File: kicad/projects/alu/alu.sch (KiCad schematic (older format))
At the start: 46 parts, among them J1 Conn_01x16_Female, J2 Conn_01x18_Female, J3 Control_signal_backplane, J4 Bus_connection, J5 Aux_connection, U1 74HCT04, U10 74HCT157, U11 74HCT157, U2 74LS181, U3 74LS181, U4 74HCT245, U5 74LS181, U6 74HCT245, U7 74LS181, U8 74HCT157, U9 74HCT157

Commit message: Add updated 74LS181 to eight bit symbol lib with open collector output. Mostly finish schematic. Little bit of PBC layout work.
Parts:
- removed U2, U3, U5, U7: 74LS181, Package_DIP:DIP-24_W15.24mm_Socket, symbol 74xx:74LS181
- added U2, U3, U5, U7: 74LS181, Package_DIP:DIP-24_W15.24mm_Socket, symbol eight-bit-computer:74LS181
- C1, C10, C11, C2, C3, C4, C5, C6, C7, C8, C9: footprint (none) -> Capacitor_THT:C_Disc_D4.7mm_W2.5mm_P5.00mm
- J1: value Conn_01x16_Female -> ACC_CONTENTS
- J2: value Conn_01x18_Female -> RES_AEQB_CRYBRW_OUT; footprint (none) -> Connector_PinSocket_2.54mm:PinSocket_1x18_P2.54mm_Horizontal
- R1: value R_US -> 1K; footprint (none) -> Resistor_THT:R_Axial_DIN0207_L6.3mm_D2.5mm_P10.16mm_Horizontal
- U10, U11, U8, U9: footprint Package_DIP:DIP-16_W7.62mm -> Package_DIP:DIP-16_W7.62mm_Socket
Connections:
- net labels added: ACC_00, ACC_01, ACC_02, ACC_03, ACC_04, ACC_05, ACC_06, ACC_07, ACC_08, ACC_09, ACC_10, ACC_11, ACC_12, ACC_13, ACC_14, ACC_15, A_EQ_B, A_IS_BUS, BUS_00, BUS_01, BUS_02, BUS_03, BUS_04, BUS_05, BUS_06, BUS_07, BUS_08, BUS_09, BUS_10, BUS_11, BUS_12, BUS_13, BUS_14, BUS_15, CARRY_BORROW_OUT, CARRY_IN, CARRY_IN_BAR, M, RES_00, RES_01, RES_02, RES_03, RES_04, RES_05, RES_06, RES_07, RES_08, RES_09, RES_10, RES_11, RES_12, RES_13, RES_14, RES_15, RES_BUF_00, RES_BUF_01, RES_BUF_02, RES_BUF_03, RES_BUF_04, RES_BUF_05, RES_BUF_06, RES_BUF_07, RES_BUF_08, RES_BUF_09, RES_BUF_10, RES_BUF_11, RES_BUF_12, RES_BUF_13, RES_BUF_14, RES_BUF_15, S0, S1, S2, S3, SEL_00, SEL_01, SEL_02, SEL_03, SEL_04, SEL_05, SEL_06, SEL_07, SEL_08, SEL_09, SEL_10, SEL_11, SEL_12, SEL_13, SEL_14, SEL_15
- wire segments 2 -> 148
- no-connect marks 0 -> 41
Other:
- moved on the sheet: C1, C10, C11, C2, C3, C4, C5, C6, C7, C8, C9, D1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

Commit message: Add LED with smaller footprint. More work on ALU PCB.
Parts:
- D1, D10, D11, D12, D13, D14, D15, D16, D2, D3, D4, D5, D6, D7, D8, D9: footprint LED_THT:LED_D5.0mm_Horizontal_O3.81mm_Z3.0mm -> eight-bit-computer:LED_D5.0mm_Horizontal_O3.81mm_Z3.0mm
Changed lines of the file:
@@
 F 0 "D16" H 4750 7000 50  0000 C CNN
 F 1 "LED" H 4550 7000 50  0000 C CNN
-F 2 "LED_THT:LED_D5.0mm_Horizontal_O3.81mm_Z3.0mm" H 5000 7050 50  0001 C CNN
+F 2 "eight-bit-computer:LED_D5.0mm_Horizontal_O3.81mm_Z3.0mm" H 5000 7050 50  0001 C CNN
 F 3 "~" H 5000 7050 50  0001 C CNN
 	1    5000 7050
@@
 F 0 "D15" H 4750 7150 50  0000 C CNN
 F 1 "LED" H 4550 7150 50  0000 C CNN
-F 2 "LED_THT:LED_D5.0mm_Horizontal_O3.81mm_Z3.0mm" H 5000 7200 50  0001 C CNN
+F 2 "eight-bit-computer:LED_D5.0mm_Horizontal_O3.81mm_Z3.0mm" H 5000 7200 50  0001 C CNN
 F 3 "~" H 5000 7200 50  0001 C CNN
 	1    5000 7200
@@
 F 0 "D14" H 4750 7300 50  0000 C CNN
 F 1 "LED" H 4550 7300 50  0000 C CNN
-F 2 "LED_THT:LED_D5.0mm_Horizontal_O3.81mm_Z3.0mm" H 5000 7350 50  0001 C CNN
+F 2 "eight-bit-computer:LED_D5.0mm_Horizontal_O3.81mm_Z3.0mm" H 5000 7350 50  0001 C CNN
 F 3 "~" H 5000 7350 50  0001 C CNN
 	1    5000 7350
@@
 F 0 "D13" H 4750 7450 50  0000 C CNN
 F 1 "LED" H 4550 7450 50  0000 C CNN
-F 2 "LED_THT:LED_D5.0mm_Horizontal_O3.81mm_Z3.0mm" H 5000 7500 50  0001 C CNN
+F 2 "eight-bit-computer:LED_D5.0mm_Horizontal_O3.81mm_Z3.0mm" H 5000 7500 50  0001 C CNN
 F 3 "~" H 5000 7500 50  0001 C CNN
 	1    5000 7500
@@
 F 0 "D12" H 4750 7600 50  0000 C CNN
 F 1 "LED" H 4550 7600 50  0000 C CNN
-F 2 "LED_THT:LED_D5.0mm_Horizontal_O3.81mm_Z3.0mm" H 5000 7650 50  0001 C CNN
+F 2 "eight-bit-computer:LED_D5.0mm_Horizontal_O3.81mm_Z3.0mm" H 5000 7650 50  0001 C CNN
 F 3 "~" H 5000 7650 50  0001 C CNN
 	1    5000 7650
@@
 F 0 "D11" H 4750 7750 50  0000 C CNN
 F 1 "LED" H 4550 7750 50  0000 C CNN
-F 2 "LED_THT:LED_D5.0mm_Horizontal_O3.81mm_Z3.0mm" H 5000 7800 50  0001 C CNN
+F 2 "eight-bit-computer:LED_D5.0mm_Horizontal_O3.81mm_Z3.0mm" H 5000 7800 50  0001 C CNN
 F 3 "~" H 5000 7800 50  0001 C CNN
 	1    5000 7800
@@
 F 0 "D10" H 4750 7900 50  0000 C CNN
 F 1 "LED" H 4550 7900 50  0000 C CNN
-F 2 "LED_THT:LED_D5.0mm_Horizontal_O3.81mm_Z3.0mm" H 5000 7950 50  0001 C CNN
+F 2 "eight-bit-computer:LED_D5.0mm_Horizontal_O3.81mm_Z3.0mm" H 5000 7950 50  0001 C CNN
 F 3 "~" H 5000 7950 50  0001 C CNN
 	1    5000 7950
@@
 F 0 "D9" H 4750 8050 50  0000 C CNN
 F 1 "LED" H 4550 8050 50  0000 C CNN
-F 2 "LED_THT:LED_D5.0mm_Horizontal_O3.81mm_Z3.0mm" H 5000 8100 50  0001 C CNN
+F 2 "eight-bit-computer:LED_D5.0mm_Horizontal_O3.81mm_Z3.0mm" H 5000 8100 50  0001 C CNN
 F 3 "~" H 5000 8100 50  0001 C CNN
 	1    5000 8100
@@
 F 0 "D8" H 4750 8200 50  0000 C CNN
 F 1 "LED" H 4550 8200 50  0000 C CNN
-F 2 "LED_THT:LED_D5.0mm_Horizontal_O3.81mm_Z3.0mm" H 5000 8250 50  0001 C CNN
+F 2 "eight-bit-computer:LED_D5.0mm_Horizontal_O3.81mm_Z3.0mm" H 5000 8250 50  0001 C CNN
 F 3 "~" H 5000 8250 50  0001 C CNN
 	1    5000 8250
@@
 F 0 "D7" H 4750 8350 50  0000 C CNN
 F 1 "LED" H 4550 8350 50  0000 C CNN
-F 2 "LED_THT:LED_D5.0mm_Horizontal_O3.81mm_Z3.0mm" H 5000 8400 50  0001 C CNN
+F 2 "eight-bit-computer:LED_D5.0mm_Horizontal_O3.81mm_Z3.0mm" H 5000 8400 50  0001 C CNN
 F 3 "~" H 5000 8400 50  0001 C CNN
 	1    5000 8400
@@
 F 0 "D6" H 4750 8500 50  0000 C CNN
 F 1 "LED" H 4550 8500 50  0000 C CNN
-F 2 "LED_THT:LED_D5.0mm_Horizontal_O3.81mm_Z3.0mm" H 5000 8550 50  0001 C CNN
+F 2 "eight-bit-computer:LED_D5.0mm_Horizontal_O3.81mm_Z3.0mm" H 5000 8550 50  0001 C CNN
 F 3 "~" H 5000 8550 50  0001 C CNN
 	1    5000 8550
@@
 F 0 "D5" H 4750 8650 50  0000 C CNN
 F 1 "LED" H 4550 8650 50  0000 C CNN
-F 2 "LED_THT:LED_D5.0mm_Horizontal_O3.81mm_Z3.0mm" H 5000 8700 50  0001 C CNN
+F 2 "eight-bit-computer:LED_D5.0mm_Horizontal_O3.81mm_Z3.0mm" H 5000 8700 50  0001 C CNN
 F 3 "~" H 5000 8700 50  0001 C CNN
 	1    5000 8700
@@
 F 0 "D4" H 4750 8800 50  0000 C CNN
 F 1 "LED" H 4550 8800 50  0000 C CNN
-F 2 "LED_THT:LED_D5.0mm_Horizontal_O3.81mm_Z3.0mm" H 5000 8850 50  0001 C CNN
+F 2 "eight-bit-computer:LED_D5.0mm_Horizontal_O3.81mm_Z3.0mm" H 5000 8850 50  0001 C CNN
 F 3 "~" H 5000 8850 50  0001 C CNN
 	1    5000 8850
@@
 F 0 "D3" H 4750 8950 50  0000 C CNN
 F 1 "LED" H 4550 8950 50  0000 C CNN
-F 2 "LED_THT:LED_D5.0mm_Horizontal_O3.81mm_Z3.0mm" H 5000 9000 50  0001 C CNN
+F 2 "eight-bit-computer:LED_D5.0mm_Horizontal_O3.81mm_Z3.0mm" H 5000 9000 50  0001 C CNN
 F 3 "~" H 5000 9000 50  0001 C CNN
 	1    5000 9000
@@
 F 0 "D2" H 4750 9100 50  0000 C CNN
 F 1 "LED" H 4550 9100 50  0000 C CNN
-F 2 "LED_THT:LED_D5.0mm_Horizontal_O3.81mm_Z3.0mm" H 5000 9150 50  0001 C CNN
+F 2 "eight-bit-computer:LED_D5.0mm_Horizontal_O3.81mm_Z3.0mm" H 5000 9150 50  0001 C CNN
 F 3 "~" H 5000 9150 50  0001 C CNN
 	1    5000 9150
@@
 F 0 "D1" H 4750 9250 50  0000 C CNN
 F 1 "LED" H 4550 9250 50  0000 C CNN
-F 2 "LED_THT:LED_D5.0mm_Horizontal_O3.81mm_Z3.0mm" H 5000 9300 50  0001 C CNN
+F 2 "eight-bit-computer:LED_D5.0mm_Horizontal_O3.81mm_Z3.0mm" H 5000 9300 50  0001 C CNN
 F 3 "~" H 5000 9300 50  0001 C CNN
 	1    5000 9300

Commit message: ALU ready for fab
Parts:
- added C12: 330uF, Capacitor_THT:CP_Radial_D6.3mm_P2.50mm, symbol Device:CP
- C1, C10, C11, C2, C3, C4, C5, C6, C7, C8, C9: value C -> 0.1uF
- J3: footprint eight-bit-computer:backplane-connector -> eight-bit-computer:backplane-connector-single-row-annotated
- J4: footprint Connector_PinHeader_2.54mm:PinHeader_1x16_P2.54mm_Horizontal -> eight-bit-computer:bus-connection
- J5: footprint Connector_PinHeader_2.54mm:PinHeader_1x10_P2.54mm_Horizontal -> eight-bit-computer:aux-connection
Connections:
- net GND: now also C12.2
- net VCC: now also C12.1
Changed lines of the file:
@@
 F 0 "J5" H 13512 8275 50  0000 C CNN
 F 1 "Aux_connection" H 13512 8184 50  0000 C CNN
-F 2 "Connector_PinHeader_2.54mm:PinHeader_1x10_P2.54mm_Horizontal" H 13600 7650 50  0001 C CNN
+F 2 "eight-bit-computer:aux-connection" H 13600 7650 50  0001 C CNN
 F 3 "~" H 13600 7650 50  0001 C CNN
 	1    13600 7650
@@
 F 0 "J4" H 12362 8425 50  0000 C CNN
 F 1 "Bus_connection" H 12362 8334 50  0000 C CNN
-F 2 "Connector_PinHeader_2.54mm:PinHeader_1x16_P2.54mm_Horizontal" H 12400 7900 50  0001 C CNN
+F 2 "eight-bit-computer:bus-connection" H 12400 7900 50  0001 C CNN
 F 3 "~" H 12400 7900 50  0001 C CNN
 	1    12500 7500
@@
 F 0 "J3" H 14887 8925 50  0000 C CNN
 F 1 "Control_signal_backplane" H 14887 8834 50  0000 C CNN
-F 2 "eight-bit-computer:backplane-connector" H 15000 7200 50  0001 C CNN
+F 2 "eight-bit-computer:backplane-connector-single-row-annotated" H 15000 7200 50  0001 C CNN
 F 3 "~" H 15000 7200 50  0001 C CNN
 	1    15000 7200
@@
 P 3950 1850
 F 0 "C2" H 4065 1896 50  0000 L CNN
-F 1 "C" H 4065 1805 50  0000 L CNN
+F 1 "0.1uF" H 4065 1805 50  0000 L CNN
 F 2 "Capacitor_THT:C_Disc_D4.7mm_W2.5mm_P5.00mm" H 3988 1700 50  0001 C CNN
 F 3 "~" H 3950 1850 50  0001 C CNN
@@
 P 6150 1850
 F 0 "C3" H 6265 1896 50  0000 L CNN
-F 1 "C" H 6265 1805 50  0000 L CNN
+F 1 "0.1uF" H 6265 1805 50  0000 L CNN
 F 2 "Capacitor_THT:C_Disc_D4.7mm_W2.5mm_P5.00mm" H 6188 1700 50  0001 C CNN
 F 3 "~" H 6150 1850 50  0001 C CNN
@@
 P 8450 1850
 F 0 "C5" H 8565 1896 50  0000 L CNN
-F 1 "C" H 8565 1805 50  0000 L CNN
+F 1 "0.1uF" H 8565 1805 50  0000 L CNN
 F 2 "Capacitor_THT:C_Disc_D4.7mm_W2.5mm_P5.00mm" H 8488 1700 50  0001 C CNN
 F 3 "~" H 8450 1850 50  0001 C CNN
@@
 P 10800 1850
 F 0 "C9" H 10915 1896 50  0000 L CNN
-F 1 "C" H 10915 1805 50  0000 L CNN
+F 1 "0.1uF" H 10915 1805 50  0000 L CNN
 F 2 "Capacitor_THT:C_Disc_D4.7mm_W2.5mm_P5.00mm" H 10838 1700 50  0001 C CNN
 F 3 "~" H 10800 1850 50  0001 C CNN
@@
 P 3800 4850
 F 0 "C8" H 3915 4896 50  0000 L CNN
-F 1 "C" H 3915 4805 50  0000 L CNN
+F 1 "0.1uF" H 3915 4805 50  0000 L CNN
 F 2 "Capacitor_THT:C_Disc_D4.7mm_W2.5mm_P5.00mm" H 3838 4700 50  0001 C CNN
 F 3 "~" H 3800 4850 50  0001 C CNN
@@
 P 6250 4900
 F 0 "C10" H 6365 4946 50  0000 L CNN
-F 1 "C" H 6365 4855 50  0000 L CNN
+F 1 "0.1uF" H 6365 4855 50  0000 L CNN
 F 2 "Capacitor_THT:C_Disc_D4.7mm_W2.5mm_P5.00mm" H 6288 4750 50  0001 C CNN
 F 3 "~" H 6250 4900 50  0001 C CNN
@@
 P 10800 4900
 F 0 "C11" H 10915 4946 50  0000 L CNN
-F 1 "C" H 10915 4855 50  0000 L CNN
+F 1 "0.1uF" H 10915 4855 50  0000 L CNN
 F 2 "Capacitor_THT:C_Disc_D4.7mm_W2.5mm_P5.00mm" H 10838 4750 50  0001 C CNN
 F 3 "~" H 10800 4900 50  0001 C CNN
@@
 P 8550 4850
 F 0 "C7" H 8665 4896 50  0000 L CNN
-F 1 "C" H 8665 4805 50  0000 L CNN
+F 1 "0.1uF" H 8665 4805 50  0000 L CNN
 F 2 "Capacitor_THT:C_Disc_D4.7mm_W2.5mm_P5.00mm" H 8588 4700 50  0001 C CNN
 F 3 "~" H 8550 4850 50  0001 C CNN
@@
 P 3900 9500
 F 0 "C6" H 4015 9546 50  0000 L CNN
-F 1 "C" H 4015 9455 50  0000 L CNN
+F 1 "0.1uF" H 4015 9455 50  0000 L CNN
 F 2 "Capacitor_THT:C_Disc_D4.7mm_W2.5mm_P5.00mm" H 3938 9350 50  0001 C CNN
 F 3 "~" H 3900 9500 50  0001 C CNN
@@
 P 13850 1250
 F 0 "C1" H 13965 1296 50  0000 L CNN
-F 1 "C" H 13965 1205 50  0000 L CNN
+F 1 "0.1uF" H 13965 1205 50  0000 L CNN
 F 2 "Capacitor_THT:C_Disc_D4.7mm_W2.5mm_P5.00mm" H 13888 1100 50  0001 C CNN
 F 3 "~" H 13850 1250 50  0001 C CNN
@@
 P 3950 7350
 F 0 "C4" H 4065 7396 50  0000 L CNN
-F 1 "C" H 4065 7305 50  0000 L CNN
+F 1 "0.1uF" H 4065 7305 50  0000 L CNN
 F 2 "Capacitor_THT:C_Disc_D4.7mm_W2.5mm_P5.00mm" H 3988 7200 50  0001 C CNN
 F 3 "~" H 3950 7350 50  0001 C CNN
@@
 L power:GND #PWR02
 U 1 1 5FA1038F
-P 9900 8100
-F 0 "#PWR02" H 9900 7850 50  0001 C CNN
-F 1 "GND" H 9905 7927 50  0000 C CNN
-F 2 "" H 9900 8100 50  0001 C CNN
-F 3 "" H 9900 8100 50  0001 C CNN
-	1    9900 8100
+P 9900 8300
+F 0 "#PWR02" H 9900 8050 50  0001 C CNN
+F 1 "GND" H 9905 8127 50  0000 C CNN
+F 2 "" H 9900 8300 50  0001 C CNN
+F 3 "" H 9900 8300 50  0001 C CNN
+	1    9900 8300
 	1    0    0    -1
 $EndComp
@@
 L power:PWR_FLAG #FLG02
 U 1 1 5FA13D2F
-P 9900 8100
-F 0 "#FLG02" H 9900 8175 50  0001 C CNN
-F 1 "PWR_FLAG" V 9900 8228 50  0000 L CNN
-F 2 "" H 9900 8100 50  0001 C CNN
-F 3 "~" H 9900 8100 50  0001 C CNN
-	1    9900 8100
+P 9900 8300
+F 0 "#FLG02" H 9900 8375 50  0001 C CNN
+F 1 "PWR_FLAG" V 9900 8428 50  0000 L CNN
+F 2 "" H 9900 8300 50  0001 C CNN
+F 3 "~" H 9900 8300 50  0001 C CNN
+	1    9900 8300
 	0    1    1    0
 $EndComp
 Text Label 9850 7950 2    50   ~ 0
 VCC
-Text Label 9850 8100 2    50   ~ 0
+Text Label 9850 8300 2    50   ~ 0
 GND
-Wire Wire Line
-	9850 7950 9900 7950
 Connection ~ 9900 7950
-Wire Wire Line
-	9850 8100 9900 8100
-Connection ~ 9900 8100
+Connection ~ 9900 8300
 Text Label 12600 6800 0    50   ~ 0
 BUS_00
@@
 	1    0    0    -1
 $EndComp
+$Comp
+L Device:CP C12
+U 1 1 5FC1FB19
+P 9250 8100
+F 0 "C12" H 9368 8146 50  0000 L CNN
+F 1 "330uF" H 9368 8055 50  0000 L CNN
+F 2 "Capacitor_THT:CP_Radial_D6.3mm_P2.50mm" H 9288 7950 50  0001 C CNN
+F 3 "~" H 9250 8100 50  0001 C CNN
+	1    9250 8100
+	1    0    0    -1
+$EndComp
+Wire Wire Line
+	9250 7950 9900 7950
+Wire Wire Line
+	9250 8250 9250 8300
+Wire Wire Line
+	9250 8300 9900 8300
 $EndSCHEMATC

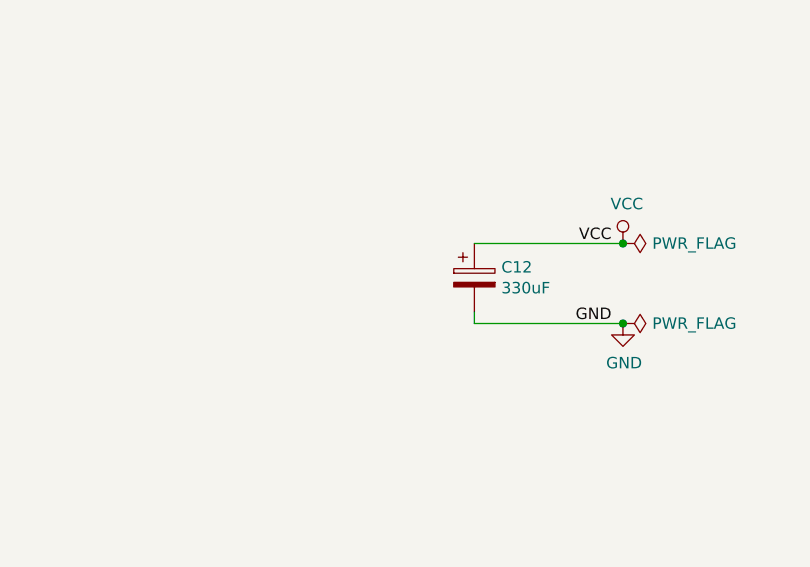
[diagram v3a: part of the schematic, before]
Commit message: Added more large caps, shrunk vias a bit
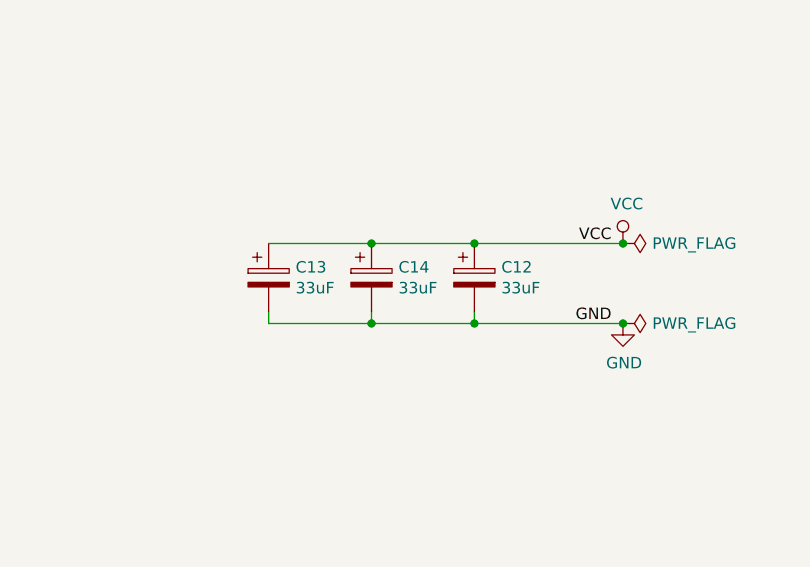
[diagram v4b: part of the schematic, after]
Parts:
- added C13, C14: 33uF, Capacitor_THT:CP_Radial_D6.3mm_P2.50mm, symbol Device:CP
- C12: value 330uF -> 33uF
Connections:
- net GND: now also C13.2, C14.2
- net VCC: now also C13.1, C14.1
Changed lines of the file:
@@
 P 9250 8100
 F 0 "C12" H 9368 8146 50  0000 L CNN
-F 1 "330uF" H 9368 8055 50  0000 L CNN
+F 1 "33uF" H 9368 8055 50  0000 L CNN
 F 2 "Capacitor_THT:CP_Radial_D6.3mm_P2.50mm" H 9288 7950 50  0001 C CNN
 F 3 "~" H 9250 8100 50  0001 C CNN
@@
 Wire Wire Line
 	9250 8300 9900 8300
+$Comp
+L Device:CP C14
+U 1 1 5FC812BA
+P 8800 8100
+F 0 "C14" H 8918 8146 50  0000 L CNN
+F 1 "33uF" H 8918 8055 50  0000 L CNN
+F 2 "Capacitor_THT:CP_Radial_D6.3mm_P2.50mm" H 8838 7950 50  0001 C CNN
+F 3 "~" H 8800 8100 50  0001 C CNN
+	1    8800 8100
+	1    0    0    -1
+$EndComp
+$Comp
+L Device:CP C13
+U 1 1 5FC81852
+P 8350 8100
+F 0 "C13" H 8468 8146 50  0000 L CNN
+F 1 "33uF" H 8468 8055 50  0000 L CNN
+F 2 "Capacitor_THT:CP_Radial_D6.3mm_P2.50mm" H 8388 7950 50  0001 C CNN
+F 3 "~" H 8350 8100 50  0001 C CNN
+	1    8350 8100
+	1    0    0    -1
+$EndComp
+Wire Wire Line
+	8350 7950 8800 7950
+Connection ~ 9250 7950
+Connection ~ 8800 7950
+Wire Wire Line
+	8800 7950 9250 7950
+Wire Wire Line
+	9250 8300 8800 8300
+Wire Wire Line
+	8350 8300 8350 8250
+Connection ~ 9250 8300
+Wire Wire Line
+	8800 8250 8800 8300
+Connection ~ 8800 8300
+Wire Wire Line
+	8800 8300 8350 8300
 $EndSCHEMATC

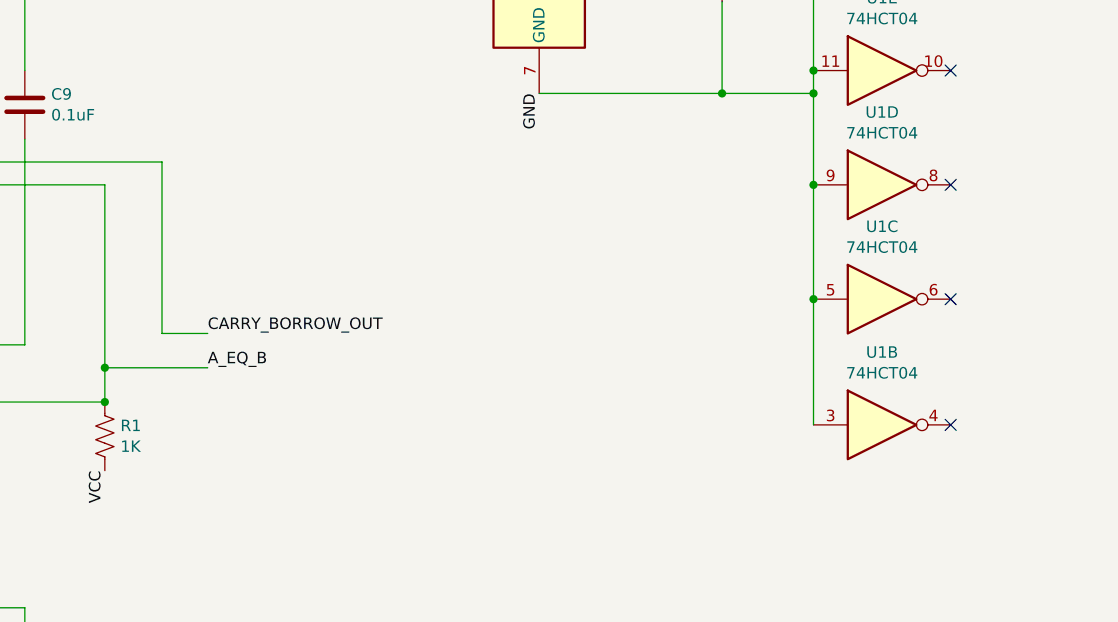
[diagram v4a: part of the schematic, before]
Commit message: Fix non-inverted carry borrow out in ALU schematic and PCB.
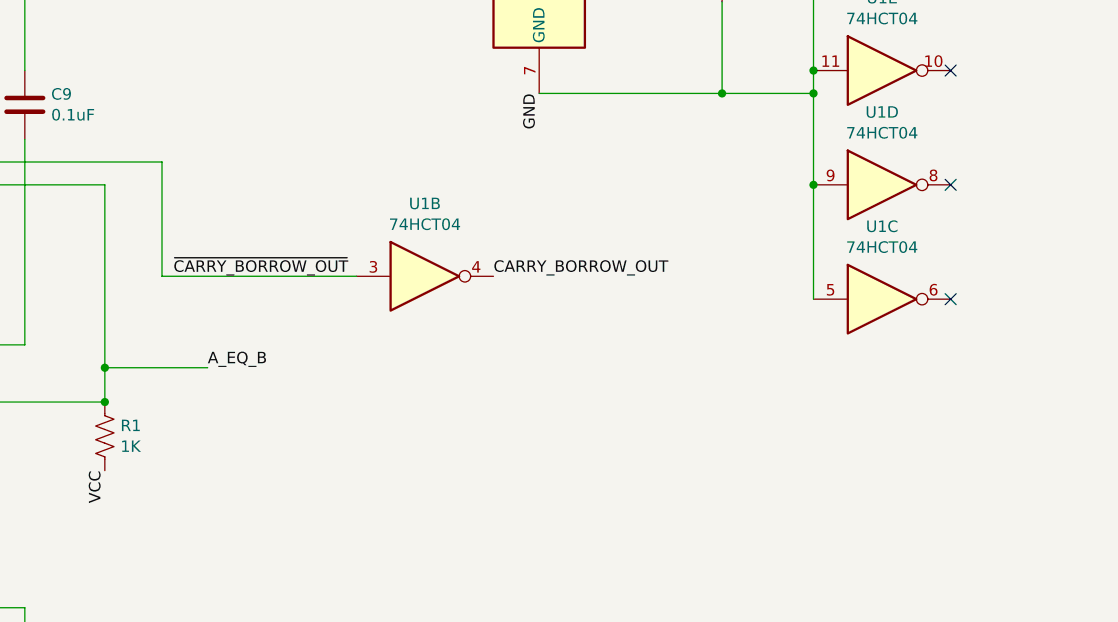
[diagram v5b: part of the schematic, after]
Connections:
- net CARRY_BORROW_OUT: now also U1.4; no longer U7.16 (Cn+4)
- net GND: no longer U1.3
- new net ~CARRY_BORROW_OUT: U1.3, U7.16 (Cn+4)
- no-connect marks 41 -> 40
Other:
- moved on the sheet: U1B
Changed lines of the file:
@@
 L 74xx:74HCT04 U1
 U 2 1 5F99F922
-P 14550 3250
-F 0 "U1" H 14550 3567 50  0000 C CNN
-F 1 "74HCT04" H 14550 3476 50  0000 C CNN
-F 2 "Package_DIP:DIP-14_W7.62mm_Socket" H 14550 3250 50  0001 C CNN
-F 3 "https://assets.nexperia.com/documents/data-sheet/74HC_HCT04.pdf" H 14550 3250 50  0001 C CNN
-	2    14550 3250
+P 12550 2600
+F 0 "U1" H 12550 2917 50  0000 C CNN
+F 1 "74HCT04" H 12550 2826 50  0000 C CNN
+F 2 "Package_DIP:DIP-14_W7.62mm_Socket" H 12550 2600 50  0001 C CNN
+F 3 "https://assets.nexperia.com/documents/data-sheet/74HC_HCT04.pdf" H 12550 2600 50  0001 C CNN
+	2    12550 2600
 	1    0    0    -1
 $EndComp
@@
 GND
 Wire Wire Line
-	11400 2850 11400 2100
+	11400 2600 11400 2100
 Wire Wire Line
 	11400 2100 10250 2100
-Text Label 11600 2850 0    50   ~ 0
+Text Label 12850 2600 0    50   ~ 0
 CARRY_BORROW_OUT
 Text Label 11150 3450 3    50   ~ 0
@@
 	11150 3000 11150 2200
 Wire Wire Line
-	11400 2850 11600 2850
+	11400 2600 12250 2600
 Text Label 9650 900  1    50   ~ 0
 VCC
@@
 Wire Wire Line
 	14250 2200 14250 2700
-Connection ~ 14250 2700
-Wire Wire Line
-	14250 2700 14250 3250
 NoConn ~ 14850 1200
 NoConn ~ 14850 1700
 NoConn ~ 14850 2200
 NoConn ~ 14850 2700
-NoConn ~ 14850 3250
 NoConn ~ 15200 5700
 NoConn ~ 15200 5800
@@
 Wire Wire Line
 	8800 8300 8350 8300
+Text Label 11450 2600 0    50   ~ 0
+~CARRY_BORROW_OUT
 $EndSCHEMATC
